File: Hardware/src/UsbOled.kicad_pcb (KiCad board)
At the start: 2 copper layers, 27.4 x 12 mm, 15 parts, among them J1 ‎USB4085, U1 16F1454

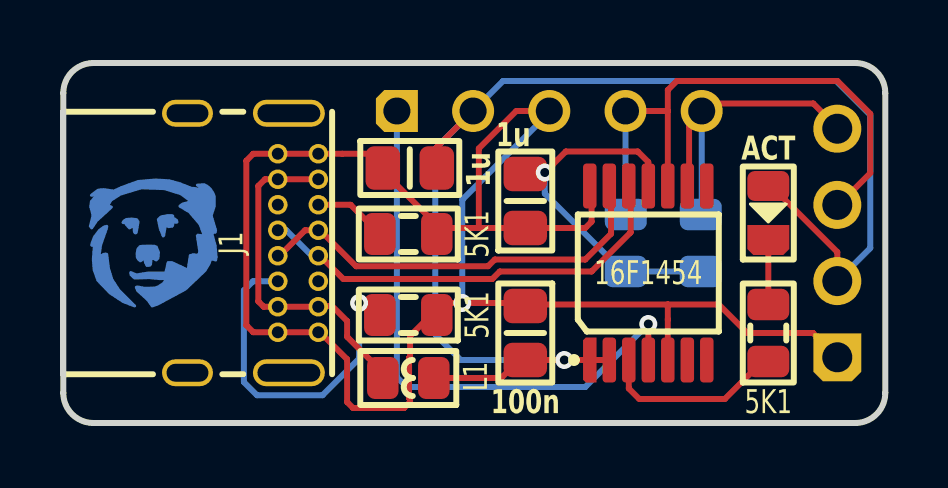
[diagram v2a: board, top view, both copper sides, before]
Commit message: Refactoring to minimum line count
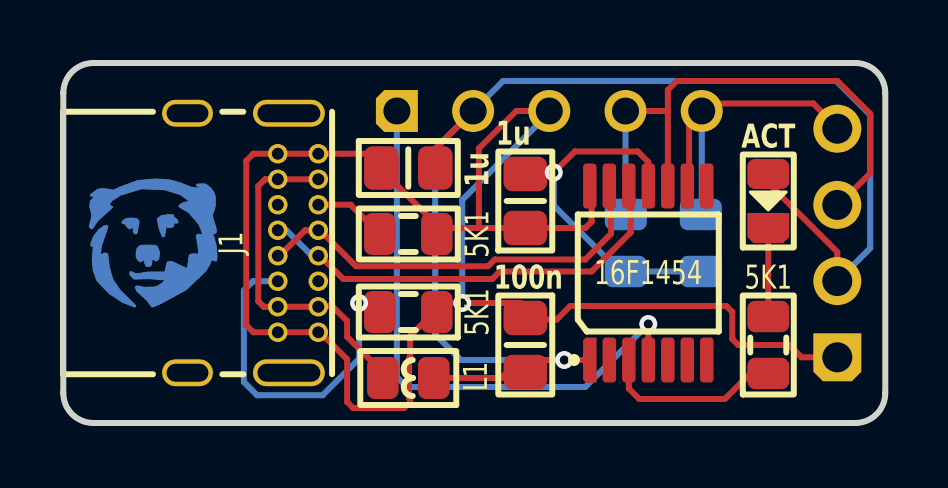
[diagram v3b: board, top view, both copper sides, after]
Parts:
- moved C1 0.40 mm to (30.4, 24.4)
- moved DS1 0.40 mm to (38.5, 19.6)
- moved R3 0.40 mm to (38.5, 24.4)
- moved R2 0.10 mm to (26.5, 23.3)
- moved C2 0.05 mm to (26.5, 18.5)
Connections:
- U1 pad 2: 5V -> (no net)
- U1 pad 5: GND -> (no net)
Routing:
- net GND: track 59.5 -> 58.0 mm
- net 5V: track 45.2 -> 44.5 mm
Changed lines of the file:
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@@
   (net 13 "OUT_LED_ACTIVE")
   (footprint "Medo64:DS (0805)" (layer "F.Cu")
-    (at 38.5 20 90)
+    (at 38.5 19.6 90)
     (descr "LEDC2013X120N")
     (attr smd)
@@
       (net 3 "5V") (thermal_bridge_angle 45))
     (pad "2" smd roundrect (at -2.9 -1.3 90) (size 1.5 0.45) (layers "F.Cu" "F.Paste" "F.Mask") (roundrect_rratio 0.25)
-      (net 3 "5V") (thermal_bridge_angle 45))
+      (thermal_bridge_angle 45))
     (pad "3" smd roundrect (at -2.9 -0.65 90) (size 1.5 0.45) (layers "F.Cu" "F.Paste" "F.Mask") (roundrect_rratio 0.25)
       (net 13 "OUT_LED_ACTIVE") (thermal_bridge_angle 45))
@@
       (net 9 "ICSP_VPP") (thermal_bridge_angle 45))
     (pad "5" smd roundrect (at -2.9 0.65 90) (size 1.5 0.45) (layers "F.Cu" "F.Paste" "F.Mask") (roundrect_rratio 0.25)
-      (net 4 "GND") (thermal_bridge_angle 45))
+      (thermal_bridge_angle 45))
     (pad "6" smd roundrect (at -2.9 1.3 90) (size 1.5 0.45) (layers "F.Cu" "F.Paste" "F.Mask") (roundrect_rratio 0.25)
       (thermal_bridge_angle 45))
@@
   (footprint "Medo64:R (0805)" (layer "F.Cu")
     (at 26.5 20.7 180)
-    (descr "RESC2013X70N")
+    (tags "RESC2013X70N")
     (attr smd)
     (fp_text reference "R1" (at 0 -1.6) (layer "F.SilkS") hide
@@
         (effects (font (size 0.8 0.6) (thickness 0.15) bold))
     )
-    (fp_text value "1u" (at 2.2 -0.4) (layer "F.SilkS")
+    (fp_text value "1u" (at 2.25 -0.4) (layer "F.SilkS")
         (effects (font (size 0.8 0.6) (thickness 0.15) bold))
     )
@@
   )
   (footprint "Medo64:C (0805)" (layer "F.Cu")
-    (at 30.4 24 -90)
+    (at 30.4 24.4 -90)
     (tags "CAPC2013X140N")
     (attr smd)
@@
         (effects (font (size 0.8 0.6) (thickness 0.15) bold))
     )
-    (fp_text value "100n" (at 2.3 0) (layer "F.SilkS")
+    (fp_text value "100n" (at -2.25 -0.1) (layer "F.SilkS")
         (effects (font (size 0.8 0.6) (thickness 0.15) bold))
     )
@@
   )
   (footprint "Medo64:R (0805)" (layer "F.Cu")
-    (at 26.5 23.4 180)
-    (descr "RESC2013X70N")
+    (at 26.5 23.3 180)
+    (tags "RESC2013X70N")
     (attr smd)
     (fp_text reference "R2" (at 0 -1.6) (layer "F.SilkS") hide
@@
   )
   (footprint "Medo64:R (0805)" (layer "F.Cu")
-    (at 38.5 24 90)
-    (descr "RESC2013X70N")
+    (at 38.5 24.4 90)
+    (tags "RESC2013X70N")
     (attr smd)
     (fp_text reference "R3" (at 0 -1.6 90) (layer "F.SilkS") hide
         (effects (font (size 0.8 0.6) (thickness 0.15)))
     )
-    (fp_text value "5K1" (at -2.3 0) (layer "F.SilkS")
+    (fp_text value "5K1" (at 2.25 0) (layer "F.SilkS")
         (effects (font (size 0.8 0.6) (thickness 0.15)))
     )
@@
   )
   (footprint "Medo64:C (0805)" (layer "F.Cu")
-    (at 26.55 18.5)
+    (at 26.5 18.5)
     (tags "CAPC2013X140N")
     (attr smd)
@@
   (segment (start 35.45 15.6) (end 40.805635 15.6) (width 0.2) (layer "F.Cu") (net 1))
   (segment (start 33.74 16.6) (end 33.74 19.99) (width 0.2) (layer "B.Cu") (net 1))
-  (segment (start 33.74 19.99) (end 33.8 20.05) (width 0.2) (layer "B.Cu") (net 1))
   (segment (start 35.86 17.08) (end 36.34 16.6) (width 0.2) (layer "F.Cu") (net 2))
   (segment (start 40 16.35) (end 40.84 17.19) (width 0.2) (layer "F.Cu") (net 2))
@@
   (segment (start 36.53 16.35) (end 40 16.35) (width 0.2) (layer "F.Cu") (net 2))
   (segment (start 36.28 16.6) (end 36.28 19.77) (width 0.2) (layer "B.Cu") (net 2))
-  (segment (start 36.28 19.77) (end 36 20.05) (width 0.2) (layer "B.Cu") (net 2))
   (segment (start 31.7 24.9) (end 32.61 24.9) (width 0.2) (layer "F.Cu") (net 3))
   (segment (start 40.8 21.3) (end 38.6 19.1) (width 0.2) (layer "F.Cu") (net 3))
@@
   (segment (start 27.35 25.5) (end 29.6 25.5) (width 0.2) (layer "F.Cu") (net 3))
   (segment (start 29.6 25.5) (end 30.2 24.9) (width 0.2) (layer "F.Cu") (net 3))
-  (segment (start 33.2 24.9) (end 32.55 24.9) (width 0.2) (layer "F.Cu") (net 3))
   (segment (start 27.45 17.81) (end 27.45 18.5) (width 0.2) (layer "F.Cu") (net 3))
   (segment (start 28.66 16.6) (end 27.45 17.81) (width 0.2) (layer "F.Cu") (net 3))
@@
   (segment (start 24.46 24.875) (end 23.56 23.975) (width 0.2) (layer "F.Cu") (net 4))
   (segment (start 23.5 18.025) (end 24.3 18.025) (width 0.2) (layer "F.Cu") (net 4))
+  (segment (start 39.2 24.4) (end 39.61 24.81) (width 0.2) (layer "F.Cu") (net 4))
+  (segment (start 39.61 24.81) (end 40.8 24.81) (width 0.2) (layer "F.Cu") (net 4))
   (segment (start 21.1 23.74) (end 21.1 18.26) (width 0.2) (layer "F.Cu") (net 4))
   (segment (start 28.85 17.85) (end 30.1 16.6) (width 0.2) (layer "F.Cu") (net 4))
-  (segment (start 30.81 23.05) (end 35.15 23.05) (width 0.2) (layer "F.Cu") (net 4))
-  (segment (start 35.15 23.55) (end 35.15 24.9) (width 0.2) (layer "F.Cu") (net 4))
-  (segment (start 36.85 23.05) (end 37.8 24) (width 0.2) (layer "F.Cu") (net 4))
   (segment (start 32.61 19.1) (end 32.61 20.29) (width 0.2) (layer "F.Cu") (net 4))
   (segment (start 28.85 20.5) (end 28.85 17.85) (width 0.2) (layer "F.Cu") (net 4))
@@
   (segment (start 26.525 24.829505) (end 26.525 26.170495) (width 0.2) (layer "F.Cu") (net 4))
   (segment (start 26.56 24.1) (end 26.56 24.794505) (width 0.2) (layer "F.Cu") (net 4))
-  (segment (start 37.8 24) (end 39.99 24) (width 0.2) (layer "F.Cu") (net 4))
+  (segment (start 37.3 23.3) (end 37.3 24.2) (width 0.2) (layer "F.Cu") (net 4))
   (segment (start 21.335 23.975) (end 21.1 23.74) (width 0.2) (layer "F.Cu") (net 4))
   (segment (start 30.1 16.6) (end 31.2 16.6) (width 0.2) (layer "F.Cu") (net 4))
-  (segment (start 35.15 23.05) (end 35.15 23.55) (width 0.2) (layer "F.Cu") (net 4))
   (segment (start 32.61 20.29) (end 32.4 20.5) (width 0.2) (layer "F.Cu") (net 4))
-  (segment (start 25.175 18.025) (end 25.65 18.5) (width 0.2) (layer "F.Cu") (net 4))
+  (segment (start 31.45 23.55) (end 31.9 23.1) (width 0.2) (layer "F.Cu") (net 4))
   (segment (start 26.36 26.5) (end 24.66 26.5) (width 0.2) (layer "F.Cu") (net 4))
-  (segment (start 39.99 24) (end 40.8 24.81) (width 0.2) (layer "F.Cu") (net 4))
+  (segment (start 37.3 24.2) (end 37.5 24.4) (width 0.2) (layer "F.Cu") (net 4))
   (segment (start 26.56 26.3) (end 26.36 26.5) (width 0.2) (layer "F.Cu") (net 4))
-  (segment (start 35.15 23.05) (end 36.85 23.05) (width 0.2) (layer "F.Cu") (net 4))
+  (segment (start 30.45 23.55) (end 31.45 23.55) (width 0.2) (layer "F.Cu") (net 4))
   (segment (start 24.46 26.3) (end 24.46 24.875) (width 0.2) (layer "F.Cu") (net 4))
   (segment (start 30.4 20.5) (end 28.85 20.5) (width 0.2) (layer "F.Cu") (net 4))
+  (segment (start 37.1 23.1) (end 37.3 23.3) (width 0.2) (layer "F.Cu") (net 4))
   (segment (start 28.85 20.5) (end 27.65 20.5) (width 0.2) (layer "F.Cu") (net 4))
   (segment (start 27.51 23) (end 30.26 23) (width 0.2) (layer "F.Cu") (net 4))
@@
   (segment (start 26.525 26.170495) (end 26.56 26.205495) (width 0.2) (layer "F.Cu") (net 4))
   (segment (start 23.56 23.975) (end 21.335 23.975) (width 0.2) (layer "F.Cu") (net 4))
+  (segment (start 31.9 23.1) (end 37.1 23.1) (width 0.2) (layer "F.Cu") (net 4))
+  (segment (start 37.5 24.4) (end 39.2 24.4) (width 0.2) (layer "F.Cu") (net 4))
   (via (at 28.3 23) (size 0.6) (drill 0.3) (layers "F.Cu" "B.Cu") (net 4))
   (segment (start 28.3 19.56) (end 31.26 16.6) (width 0.2) (layer "B.Cu") (net 4))
@@
   (segment (start 21.725 18.875) (end 23.56 18.875) (width 0.2) (layer "F.Cu") (net 5))
   (segment (start 21.5 22.945) (end 21.5 19.1) (width 0.2) (layer "F.Cu") (net 5))
-  (segment (start 31.75 17.95) (end 31.05 18.65) (width 0.2) (layer "F.Cu") (net 6))
+  (segment (start 34.5 18.3) (end 34.15 17.95) (width 0.2) (layer "F.Cu") (net 6))
   (segment (start 31.2 18.7) (end 31.294314 18.605686) (width 0.2) (layer "F.Cu") (net 6))
-  (segment (start 34.5 18.3) (end 34.15 17.95) (width 0.2) (layer "F.Cu") (net 6))
   (segment (start 31.294314 18.605686) (end 30.96 18.605686) (width 0.2) (layer "F.Cu") (net 6))
   (segment (start 30.4 18.7) (end 31.2 18.7) (width 0.2) (layer "F.Cu") (net 6))
-  (segment (start 34.15 17.95) (end 31.75 17.95) (width 0.2) (layer "F.Cu") (net 6))
+  (segment (start 34.15 17.95) (end 32.05 17.95) (width 0.2) (layer "F.Cu") (net 6))
+  (segment (start 31.35 18.65) (end 30.45 18.65) (width 0.2) (layer "F.Cu") (net 6))
+  (segment (start 32.05 17.95) (end 31.35 18.65) (width 0.2) (layer "F.Cu") (net 6))
   (segment (start 34.5 19.1) (end 34.5 18.3) (width 0.2) (layer "F.Cu") (net 6))
-  (via (at 31.05 18.65) (size 0.6) (drill 0.3) (layers "F.Cu" "B.Cu") (net 6))
-  (segment (start 33.65 21.95) (end 33.75 21.95) (width 0.2) (layer "B.Cu") (net 6))
-  (segment (start 31.05 18.65) (end 31.05 19.35) (width 0.2) (layer "B.Cu") (net 6))
+  (via (at 31.35 18.65) (size 0.6) (drill 0.3) (layers "F.Cu" "B.Cu") (net 6))
+  (segment (start 31.35 19.75) (end 33.55 21.95) (width 0.2) (layer "B.Cu") (net 6))
+  (segment (start 31.35 18.65) (end 31.35 19.75) (width 0.2) (layer "B.Cu") (net 6))
   (segment (start 36.25 21.95) (end 33.75 21.95) (width 0.2) (layer "B.Cu") (net 6))
-  (segment (start 31.05 19.35) (end 33.65 21.95) (width 0.2) (layer "B.Cu") (net 6))
   (segment (start 32.4 21.55) (end 29.384314 21.55) (width 0.2) (layer "F.Cu") (net 7))
   (segment (start 33.26 19.1) (end 33.26 20.69) (width 0.2) (layer "F.Cu") (net 7))

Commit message: Changing LED setup
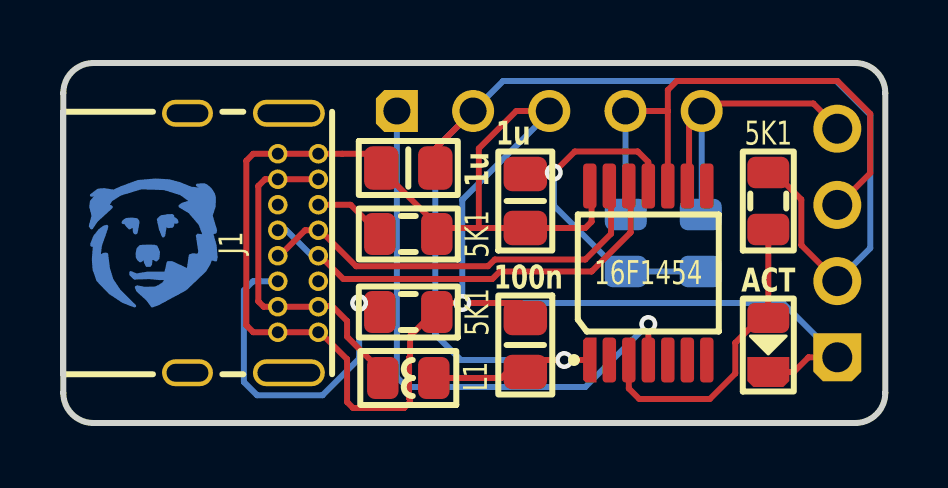
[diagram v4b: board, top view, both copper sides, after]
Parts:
- moved DS1 4.80 mm to (38.5, 24.4)
- moved R3 4.80 mm to (38.5, 19.6)
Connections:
- DS1 pad 1: LED_ACTIVE -> GND
- DS1 pad 2: 5V -> OUT_LED_ACTIVE
- R3 pad 2: LED_ACTIVE -> 5V
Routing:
- net OUT_LED_ACTIVE: track 6.06 -> 10.1 mm
- net GND: track 58.0 -> 62.0 mm
- net LED_ACTIVE: track 2.15 -> 0.00 mm
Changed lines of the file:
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@@
   (net 10 "USB_CC1")
   (net 11 "USB_CC2")
-  (net 12 "LED_ACTIVE")
-  (net 13 "OUT_LED_ACTIVE")
+  (net 12 "OUT_LED_ACTIVE")
   (footprint "Medo64:DS (0805)" (layer "F.Cu")
-    (at 38.5 19.6 90)
+    (at 38.5 24.4 90)
     (descr "LEDC2013X120N")
     (attr smd)
@@
     (pad "1" smd roundrect (at -0.9 0 90) (size 1 1.4) (layers "F.Cu" "F.Paste" "F.Mask") (roundrect_rratio 0.25)
       (chamfer_ratio 0.2) (chamfer top_left bottom_left)
-      (net 12 "LED_ACTIVE") (thermal_bridge_angle 45))
+      (net 4 "GND") (thermal_bridge_angle 45))
     (pad "2" smd roundrect (at 0.9 0 90) (size 1 1.4) (layers "F.Cu" "F.Paste" "F.Mask") (roundrect_rratio 0.25)
-      (net 3 "5V") (thermal_bridge_angle 45))
+      (net 12 "OUT_LED_ACTIVE") (thermal_bridge_angle 45))
     (model ":KICAD7_3DMODEL_DIR:LED_SMD.3dshapes/LED_0805_2012Metric.step"
       (offset (xyz 0 0 0))
@@
       (thermal_bridge_angle 45))
     (pad "3" smd roundrect (at -2.9 -0.65 90) (size 1.5 0.45) (layers "F.Cu" "F.Paste" "F.Mask") (roundrect_rratio 0.25)
-      (net 13 "OUT_LED_ACTIVE") (thermal_bridge_angle 45))
+      (net 12 "OUT_LED_ACTIVE") (thermal_bridge_angle 45))
     (pad "4" smd roundrect (at -2.9 0 90) (size 1.5 0.45) (layers "F.Cu" "F.Paste" "F.Mask") (roundrect_rratio 0.25)
       (net 9 "ICSP_VPP") (thermal_bridge_angle 45))
@@
   )
   (footprint "Medo64:R (0805)" (layer "F.Cu")
-    (at 38.5 24.4 90)
+    (at 38.5 19.6 90)
     (tags "RESC2013X70N")
     (attr smd)
@@
       (stroke (width 0.01) (type dash_dot)) (fill none) (layer "F.Fab"))
     (pad "1" smd roundrect (at -0.95 0 90) (size 1.05 1.4) (layers "F.Cu" "F.Paste" "F.Mask") (roundrect_rratio 0.25)
-      (net 13 "OUT_LED_ACTIVE") (thermal_bridge_angle 45))
+      (net 12 "OUT_LED_ACTIVE") (thermal_bridge_angle 45))
     (pad "2" smd roundrect (at 0.95 0 90) (size 1.05 1.4) (layers "F.Cu" "F.Paste" "F.Mask") (roundrect_rratio 0.25)
-      (net 12 "LED_ACTIVE") (thermal_bridge_angle 45))
+      (net 3 "5V") (thermal_bridge_angle 45))
     (model ":KICAD7_3DMODEL_DIR:Resistor_SMD.3dshapes/R_0805_2012Metric.step"
       (offset (xyz 0 0 0))
@@
   (segment (start 36.28 16.6) (end 36.28 19.77) (width 0.2) (layer "B.Cu") (net 2))
   (segment (start 31.7 24.9) (end 32.61 24.9) (width 0.2) (layer "F.Cu") (net 3))
-  (segment (start 40.8 21.3) (end 38.6 19.1) (width 0.2) (layer "F.Cu") (net 3))
+  (segment (start 38.7 18.65) (end 39.6 19.55) (width 0.2) (layer "F.Cu") (net 3))
+  (segment (start 39.6 19.55) (end 39.6 21.07) (width 0.2) (layer "F.Cu") (net 3))
   (segment (start 30.4 24.9) (end 31.7 24.9) (width 0.2) (layer "F.Cu") (net 3))
-  (segment (start 40.8 22.27) (end 40.8 21.3) (width 0.2) (layer "F.Cu") (net 3))
   (segment (start 27.35 25.5) (end 29.6 25.5) (width 0.2) (layer "F.Cu") (net 3))
   (segment (start 29.6 25.5) (end 30.2 24.9) (width 0.2) (layer "F.Cu") (net 3))
   (segment (start 27.45 17.81) (end 27.45 18.5) (width 0.2) (layer "F.Cu") (net 3))
   (segment (start 28.66 16.6) (end 27.45 17.81) (width 0.2) (layer "F.Cu") (net 3))
+  (segment (start 39.6 21.07) (end 40.8 22.27) (width 0.2) (layer "F.Cu") (net 3))
   (via (at 31.7 24.9) (size 0.6) (drill 0.3) (layers "F.Cu" "B.Cu") (net 3))
   (segment (start 40.8 22.27) (end 41.9 21.17) (width 0.2) (layer "B.Cu") (net 3))
@@
   (segment (start 27.51 23.15) (end 26.56 24.1) (width 0.2) (layer "F.Cu") (net 4))
   (segment (start 26.56 26.205495) (end 26.56 26.3) (width 0.2) (layer "F.Cu") (net 4))
+  (segment (start 38.5 25.3) (end 39.35 25.3) (width 0.2) (layer "F.Cu") (net 4))
   (segment (start 24.46 24.875) (end 23.56 23.975) (width 0.2) (layer "F.Cu") (net 4))
   (segment (start 23.5 18.025) (end 24.3 18.025) (width 0.2) (layer "F.Cu") (net 4))
-  (segment (start 39.2 24.4) (end 39.61 24.81) (width 0.2) (layer "F.Cu") (net 4))
-  (segment (start 39.61 24.81) (end 40.8 24.81) (width 0.2) (layer "F.Cu") (net 4))
   (segment (start 21.1 23.74) (end 21.1 18.26) (width 0.2) (layer "F.Cu") (net 4))
   (segment (start 28.85 17.85) (end 30.1 16.6) (width 0.2) (layer "F.Cu") (net 4))
+  (segment (start 39.84 24.81) (end 40.8 24.81) (width 0.2) (layer "F.Cu") (net 4))
   (segment (start 32.61 19.1) (end 32.61 20.29) (width 0.2) (layer "F.Cu") (net 4))
   (segment (start 28.85 20.5) (end 28.85 17.85) (width 0.2) (layer "F.Cu") (net 4))
@@
   (segment (start 26.525 24.829505) (end 26.525 26.170495) (width 0.2) (layer "F.Cu") (net 4))
   (segment (start 26.56 24.1) (end 26.56 24.794505) (width 0.2) (layer "F.Cu") (net 4))
-  (segment (start 37.3 23.3) (end 37.3 24.2) (width 0.2) (layer "F.Cu") (net 4))
+  (segment (start 39.35 25.3) (end 39.84 24.81) (width 0.2) (layer "F.Cu") (net 4))
   (segment (start 21.335 23.975) (end 21.1 23.74) (width 0.2) (layer "F.Cu") (net 4))
   (segment (start 30.1 16.6) (end 31.2 16.6) (width 0.2) (layer "F.Cu") (net 4))
   (segment (start 32.61 20.29) (end 32.4 20.5) (width 0.2) (layer "F.Cu") (net 4))
-  (segment (start 31.45 23.55) (end 31.9 23.1) (width 0.2) (layer "F.Cu") (net 4))
   (segment (start 26.36 26.5) (end 24.66 26.5) (width 0.2) (layer "F.Cu") (net 4))
-  (segment (start 37.3 24.2) (end 37.5 24.4) (width 0.2) (layer "F.Cu") (net 4))
   (segment (start 26.56 26.3) (end 26.36 26.5) (width 0.2) (layer "F.Cu") (net 4))
-  (segment (start 30.45 23.55) (end 31.45 23.55) (width 0.2) (layer "F.Cu") (net 4))
   (segment (start 24.46 26.3) (end 24.46 24.875) (width 0.2) (layer "F.Cu") (net 4))
   (segment (start 30.4 20.5) (end 28.85 20.5) (width 0.2) (layer "F.Cu") (net 4))
-  (segment (start 37.1 23.1) (end 37.3 23.3) (width 0.2) (layer "F.Cu") (net 4))
   (segment (start 28.85 20.5) (end 27.65 20.5) (width 0.2) (layer "F.Cu") (net 4))
   (segment (start 27.51 23) (end 30.26 23) (width 0.2) (layer "F.Cu") (net 4))
@@
   (segment (start 26.525 26.170495) (end 26.56 26.205495) (width 0.2) (layer "F.Cu") (net 4))
   (segment (start 23.56 23.975) (end 21.335 23.975) (width 0.2) (layer "F.Cu") (net 4))
-  (segment (start 31.9 23.1) (end 37.1 23.1) (width 0.2) (layer "F.Cu") (net 4))
-  (segment (start 37.5 24.4) (end 39.2 24.4) (width 0.2) (layer "F.Cu") (net 4))
   (via (at 28.3 23) (size 0.6) (drill 0.3) (layers "F.Cu" "B.Cu") (net 4))
   (segment (start 28.3 19.56) (end 31.26 16.6) (width 0.2) (layer "B.Cu") (net 4))
+  (segment (start 38.99 23) (end 40.8 24.81) (width 0.2) (layer "B.Cu") (net 4))
+  (segment (start 28.3 23) (end 38.99 23) (width 0.2) (layer "B.Cu") (net 4))
   (segment (start 28.3 23) (end 28.3 19.56) (width 0.2) (layer "B.Cu") (net 4))
   (segment (start 24.46 24.125) (end 25.71 25.375) (width 0.2) (layer "F.Cu") (net 5))
@@
   (segment (start 21.45934 26.075) (end 23.64066 26.075) (width 0.2) (layer "B.Cu") (net 11))
   (segment (start 21.325 22.275) (end 21.02 22.58) (width 0.2) (layer "B.Cu") (net 11))
-  (segment (start 38.5 20.9) (end 38.5 23.05) (width 0.2) (layer "F.Cu") (net 12))
-  (segment (start 34.2 26.2) (end 33.85 25.85) (width 0.2) (layer "F.Cu") (net 13))
-  (segment (start 33.85 25.85) (end 33.85 24.9) (width 0.2) (layer "F.Cu") (net 13))
-  (segment (start 37.05 26.2) (end 34.2 26.2) (width 0.2) (layer "F.Cu") (net 13))
-  (segment (start 38.3 24.95) (end 37.05 26.2) (width 0.2) (layer "F.Cu") (net 13))
+  (segment (start 38.225 23.5) (end 37.4 24.325) (width 0.2) (layer "F.Cu") (net 12))
+  (segment (start 33.85 25.85) (end 33.85 24.9) (width 0.2) (layer "F.Cu") (net 12))
+  (segment (start 34.2 26.2) (end 33.85 25.85) (width 0.2) (layer "F.Cu") (net 12))
+  (segment (start 36.55 26.2) (end 34.2 26.2) (width 0.2) (layer "F.Cu") (net 12))
+  (segment (start 37.4 24.325) (end 37.4 25.35) (width 0.2) (layer "F.Cu") (net 12))
+  (segment (start 38.5 20.55) (end 38.5 23.5) (width 0.2) (layer "F.Cu") (net 12))
+  (segment (start 37.4 25.35) (end 36.55 26.2) (width 0.2) (layer "F.Cu") (net 12))
 )
